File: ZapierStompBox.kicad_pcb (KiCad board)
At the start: 2 copper layers, 40 x 40 mm, 20 parts, among them J1 USB_B, J2 AVR-ISP-6, U1 ATmega16U2-AU, Y1 16Mhz

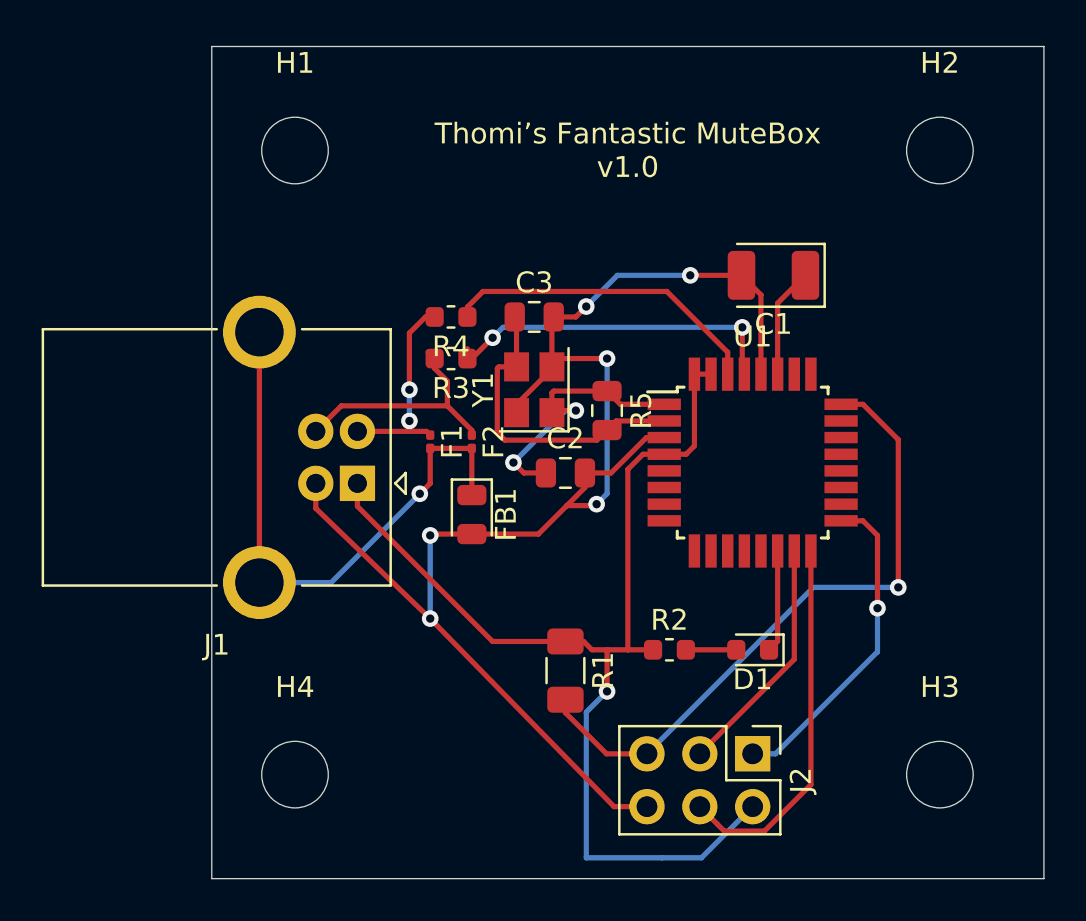
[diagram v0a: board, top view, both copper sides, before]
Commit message: Fix package for uC, re-work component placement.
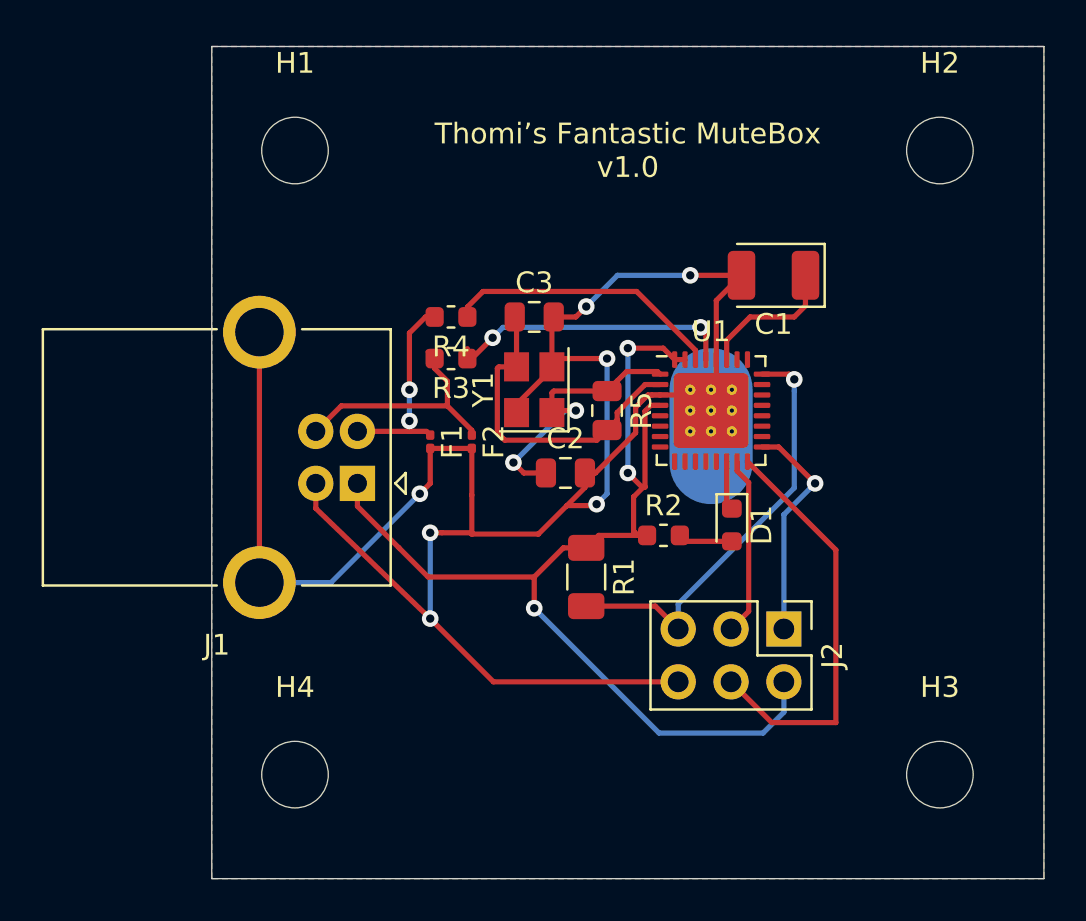
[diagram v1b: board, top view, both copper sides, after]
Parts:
- removed FB1: Ferrite_Bead, Diode_SMD:D_0805_2012Metric
- U1: footprint Package_QFP:TQFP-32_7x7mm_P0.8mm -> Package_DFN_QFN:QFN-32-1EP_5x5mm_P0.5mm_EP3.6x3.6mm_ThermalVias
- moved J2 6.18 mm to (392.5, -57.0)
- moved D1 6.08 mm to (390.0, -62.0), turned to 270 degrees
- moved R2 5.51 mm to (386.7, -61.5)
- moved R1 4.61 mm to (383.0, -59.5)
- moved U1 3.20 mm to (389.0, -67.5)
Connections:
- F1 pad 2: Net-(F1-Pad2) -> GND
- F2 pad 2: Net-(F1-Pad2) -> GND
- J1 pad 5: Net-(F1-Pad2) -> GND
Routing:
- net GND: track 72.5 -> 108.6 mm, vias 6 -> 7
- net Net-(F1-Pad2): track 28.1 -> 0.00 mm, vias 1 -> 0
- net Net-(J2-Pad5): track 31.3 -> 20.8 mm
- net Net-(J2-Pad1): track 15.7 -> 10.9 mm
- net Net-(J2-Pad3): track 11.6 -> 8.63 mm
- net Net-(R3-Pad1): track 16.6 -> 14.0 mm
- net Net-(D1-Pad1): track 4.92 -> 2.37 mm
- net Net-(R4-Pad1): track 15.6 -> 13.4 mm
- net Net-(J2-Pad4): track 18.0 -> 20.2 mm
- net Net-(C1-Pad1): track 5.30 -> 6.86 mm
- net VCC: track 54.2 -> 52.8 mm, vias 1 -> 3
- net Net-(C3-Pad1): track 15.0 -> 15.8 mm
- added copper zone on B.Cu, net GND
- added copper zone on F.Cu, net GND

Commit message: Some component changes.
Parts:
- C1: footprint Capacitor_Tantalum_SMD:CP_EIA-3528-15_AVX-H -> Capacitor_SMD:C_1206_3216Metric
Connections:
- U1 pad 33: GND -> (no net)
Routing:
- net GND: track 108.6 -> 95.4 mm, vias 7 -> 6
